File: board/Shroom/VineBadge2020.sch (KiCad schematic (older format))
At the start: 65 parts, among them IC1 ATTINY20-X, J1 CONN-TAGCONNECT-TC2050

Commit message: sending off gerbers
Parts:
- removed TP_BATT1, TP_GND1: TEST, Pin_Headers:Pin_Header_Straight_1x01, symbol TEST
- added TEST1: TP_TCK, VineBadge2020:TestPoint_Pad_2.5x2.5mm, symbol TEST
- added TEST2: TP_TDI, VineBadge2020:TestPoint_Pad_2.5x2.5mm, symbol TEST
- added TEST3: TP_RST, VineBadge2020:TestPoint_Pad_2.5x2.5mm, symbol TEST
- BT1: footprint vine_badge:COINCELL_20MM -> VineBadge2020:COINCELL_20MM_HANDSOLDER
- IC1: footprint spang_badge:ATTINY20_SOIC-14 -> VineBadge2020:ATTINY20_SOIC-14-HANDSOLDER
- J1: footprint vine_badge:TC2050-All_Holes -> VineBadge2020:TC2050-All_Holes
- SW1: renamed from SW?; footprint (none) -> VineBadge2020:JS202011JAQN-Handsolder
- SW2: renamed from SW?; footprint (none) -> VineBadge2020:SW_SPST_EVQPE1_Handsolder
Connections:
- net RST: now also TEST3.1
- net TCK: now also TEST1.1
- net TDI: now also TEST2.1
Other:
- note added: "0.3"
- note added: "11/27/2019"
- note removed: "0.1"
- note removed: "7/2/2019"
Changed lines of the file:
@@
 LIBS:VineBadge2020
 LIBS:switches
+LIBS:VineBadge2020-cache
 EELAYER 25 0
 EELAYER END
@@
 F 0 "IC1" H 2350 2850 50  0000 C CNN
 F 1 "ATTINY20-X" H 4100 1350 50  0000 C CNN
-F 2 "spang_badge:ATTINY20_SOIC-14" H 3300 2200 50  0000 C CIN
+F 2 "VineBadge2020:ATTINY20_SOIC-14-HANDSOLDER" H 3300 2200 50  0000 C CIN
 F 3 "" H 3300 2100 50  0000 C CNN
 	1    3300 2100
@@
 F 0 "BT1" H 1750 3650 50  0000 L CNN
 F 1 "Battery_Cell" H 1750 3550 50  0000 L CNN
-F 2 "vine_badge:COINCELL_20MM" V 1650 3610 50  0001 C CNN
+F 2 "VineBadge2020:COINCELL_20MM_HANDSOLDER" V 1650 3610 50  0001 C CNN
 F 3 "" V 1650 3610 50  0000 C CNN
 	1    1650 3550
@@
 Vinesauce TMG 2020 Badge
 Text Notes 16100 5650 0    60   ~ 12
-7/2/2019
+11/27/2019
 Text Notes 18550 5650 0    60   ~ 12
-0.1
+0.3
 $Comp
 L CONN-TAGCONNECT-TC2050 J1
@@
 F 0 "J1" H 5550 4450 50  0000 C CNN
 F 1 "CONN-TAGCONNECT-TC2050" H 5550 4350 50  0000 C CNN
-F 2 "vine_badge:TC2050-All_Holes" H 5400 4200 50  0001 C CNN
+F 2 "VineBadge2020:TC2050-All_Holes" H 5400 4200 50  0001 C CNN
 F 3 "" H 5400 4200 50  0000 C CNN
 	1    5550 4000
@@
 Wire Wire Line
 	3350 3350 3150 3350
-$Comp
-L TEST TP_BATT1
-U 1 1 5DDB3DBD
-P 1650 3250
-F 0 "TP_BATT1" H 1650 3550 50  0000 C BNN
-F 1 "TEST" H 1650 3500 50  0000 C CNN
-F 2 "Pin_Headers:Pin_Header_Straight_1x01" H 1650 3250 50  0001 C CNN
-F 3 "" H 1650 3250 50  0000 C CNN
-	1    1650 3250
-	1    0    0    -1
-$EndComp
-$Comp
-L TEST TP_GND1
-U 1 1 5DDB472A
-P 1650 3650
-F 0 "TP_GND1" H 1650 3950 50  0000 C BNN
-F 1 "TEST" H 1650 3900 50  0000 C CNN
-F 2 "Pin_Headers:Pin_Header_Straight_1x01" H 1650 3650 50  0001 C CNN
-F 3 "" H 1650 3650 50  0000 C CNN
-	1    1650 3650
-	-1   0    0    1
-$EndComp
 Wire Wire Line
 	2550 3150 2850 3150
 $Comp
-L SW_SPDT SW?
+L SW_SPDT SW1
 U 1 1 5DDE22CA
 P 2350 3250
-F 0 "SW?" H 2350 3420 50  0000 C CNN
+F 0 "SW1" H 2350 3420 50  0000 C CNN
 F 1 "SW_SPDT" H 2350 3050 50  0000 C CNN
-F 2 "" H 2350 3250 50  0000 C CNN
+F 2 "VineBadge2020:JS202011JAQN-Handsolder" H 2350 3250 50  0001 C CNN
 F 3 "" H 2350 3250 50  0000 C CNN
 	1    2350 3250
@@
 $EndComp
 $Comp
-L SW_Push SW?
+L SW_Push SW2
 U 1 1 5DDE23FD
 P 2900 4850
-F 0 "SW?" H 2950 4950 50  0000 L CNN
+F 0 "SW2" H 2950 4950 50  0000 L CNN
 F 1 "SW_Push" H 2900 4790 50  0000 C CNN
-F 2 "" H 2900 5050 50  0000 C CNN
+F 2 "VineBadge2020:SW_SPST_EVQPE1_Handsolder" H 2900 5050 50  0001 C CNN
 F 3 "" H 2900 5050 50  0000 C CNN
 	1    2900 4850
 	1    0    0    -1
 $EndComp
+$Comp
+L TEST TEST1
+U 1 1 5DDF1D9A
+P 5300 2400
+F 0 "TEST1" V 5300 3000 50  0000 C BNN
+F 1 "TP_TCK" V 5300 2750 50  0000 C CNN
+F 2 "VineBadge2020:TestPoint_Pad_2.5x2.5mm" H 5300 2400 50  0001 C CNN
+F 3 "" H 5300 2400 50  0000 C CNN
+	1    5300 2400
+	0    1    1    0
+$EndComp
+$Comp
+L TEST TEST2
+U 1 1 5DDF26FA
+P 5300 2500
+F 0 "TEST2" V 5300 3100 50  0000 C BNN
+F 1 "TP_TDI" V 5300 2850 50  0000 C CNN
+F 2 "VineBadge2020:TestPoint_Pad_2.5x2.5mm" H 5300 2500 50  0001 C CNN
+F 3 "" H 5300 2500 50  0000 C CNN
+	1    5300 2500
+	0    1    1    0
+$EndComp
+$Comp
+L TEST TEST3
+U 1 1 5DDF27D3
+P 5300 2600
+F 0 "TEST3" V 5300 3200 50  0000 C BNN
+F 1 "TP_RST" V 5300 2950 50  0000 C CNN
+F 2 "VineBadge2020:TestPoint_Pad_2.5x2.5mm" H 5300 2600 50  0001 C CNN
+F 3 "" H 5300 2600 50  0000 C CNN
+	1    5300 2600
+	0    1    1    0
+$EndComp
 $EndSCHEMATC

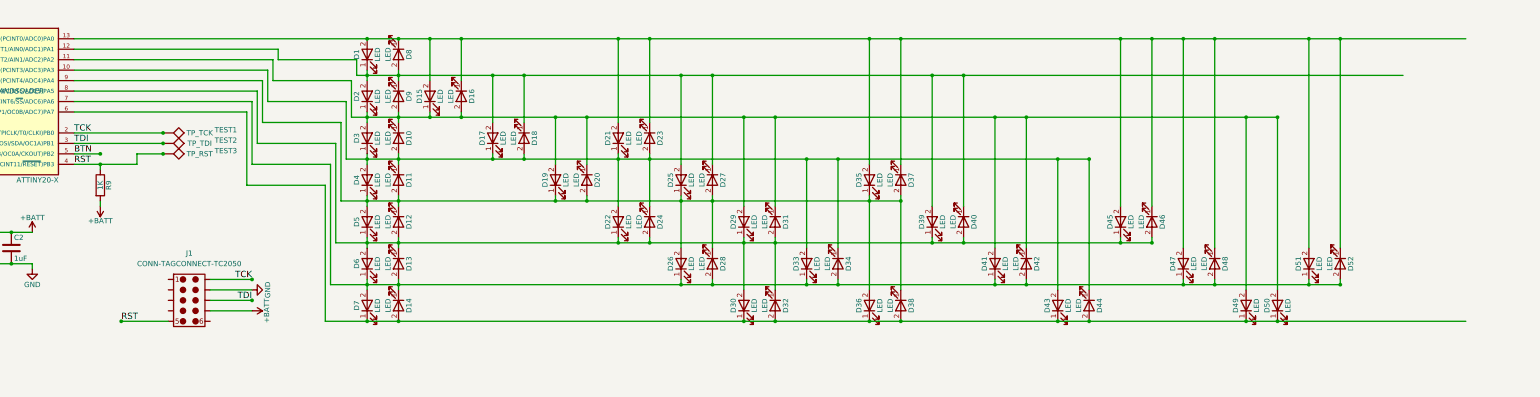
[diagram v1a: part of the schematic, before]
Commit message: added a list of LED settings
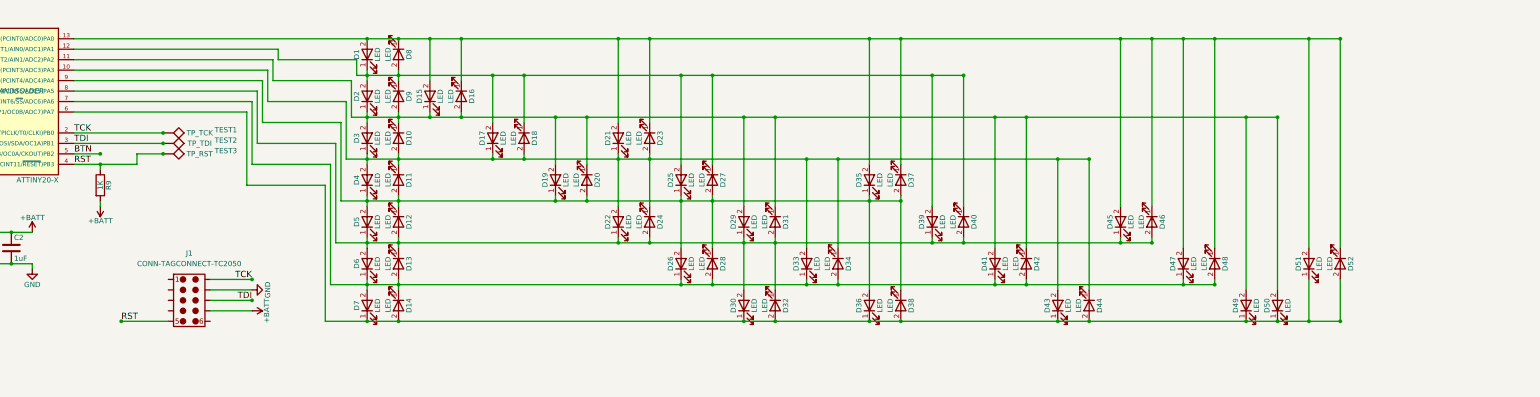
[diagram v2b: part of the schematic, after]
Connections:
- net at D14.2 (A), D30.1 (K), D32.2 (A)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: now also D51.1 (K), D52.2 (A)
- net at D13.2 (A), D14.1 (K), D26.1 (K)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: no longer D51.1 (K), D52.2 (A)
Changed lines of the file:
@@
 	2050 2750 2050 2700
-Wire Wire Line
-	4450 1500 17750 1500
 Wire Wire Line
 	4450 1600 6400 1600
@@
 	16550 1500 16550 3500
 Connection ~ 16550 1500
-Wire Wire Line
-	16550 3850 16550 3800
-Connection ~ 16550 3850
 Connection ~ 7550 1500
 Wire Wire Line
@@
 Connection ~ 8150 2250
 Wire Wire Line
-	8450 2300 8450 1850
+	8450 1850 8450 2300
 Connection ~ 8450 1850
 Wire Wire Line
@@
 Connection ~ 8450 2650
 Wire Wire Line
-	8750 2300 8750 1850
+	8750 1850 8750 2300
 Connection ~ 8750 1850
 Wire Wire Line
@@
 Connection ~ 9650 3450
 Wire Wire Line
-	10250 2700 10250 1850
+	10250 1850 10250 2700
 Connection ~ 10250 1850
 Wire Wire Line
-	10550 2700 10550 1850
+	10550 1850 10550 2700
 Connection ~ 10550 1850
 Wire Wire Line
@@
 	10550 3850 10550 3800
 Connection ~ 10550 3850
-Wire Wire Line
-	6850 4200 17750 4200
 Connection ~ 11150 4200
 Connection ~ 10850 4200
@@
 Connection ~ 12350 1500
 Wire Wire Line
-	12650 3100 12650 1850
+	12650 1850 12650 3100
 Connection ~ 12650 1850
 Wire Wire Line
-	12950 3100 12950 1850
+	12950 1850 12950 3100
 Connection ~ 12950 1850
 Wire Wire Line
@@
 	7100 2250 15950 2250
 Wire Wire Line
-	16250 3850 16250 3800
-Connection ~ 16250 3850
-Wire Wire Line
 	16250 1500 16250 3500
 Connection ~ 16250 1500
-Wire Wire Line
-	6900 3850 16550 3850
-Wire Wire Line
-	7150 1850 17150 1850
 Connection ~ 7550 4200
 Wire Wire Line
@@
 	0    1    1    0
 $EndComp
+Wire Wire Line
+	6900 3850 15350 3850
+Wire Wire Line
+	16250 3800 16250 4200
+Connection ~ 16250 4200
+Wire Wire Line
+	16550 3800 16550 4200
+Connection ~ 16550 4200
+Wire Wire Line
+	7150 1850 12950 1850
+Wire Wire Line
+	4450 1500 16550 1500
+Wire Wire Line
+	16550 4200 6850 4200
 $EndSCHEMATC
